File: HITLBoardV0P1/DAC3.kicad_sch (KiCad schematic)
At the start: 13 parts, among them U16 NC7SZ04P5X, U17 SN74LVC1G08DCKR, U18 DAC7750IPWPR

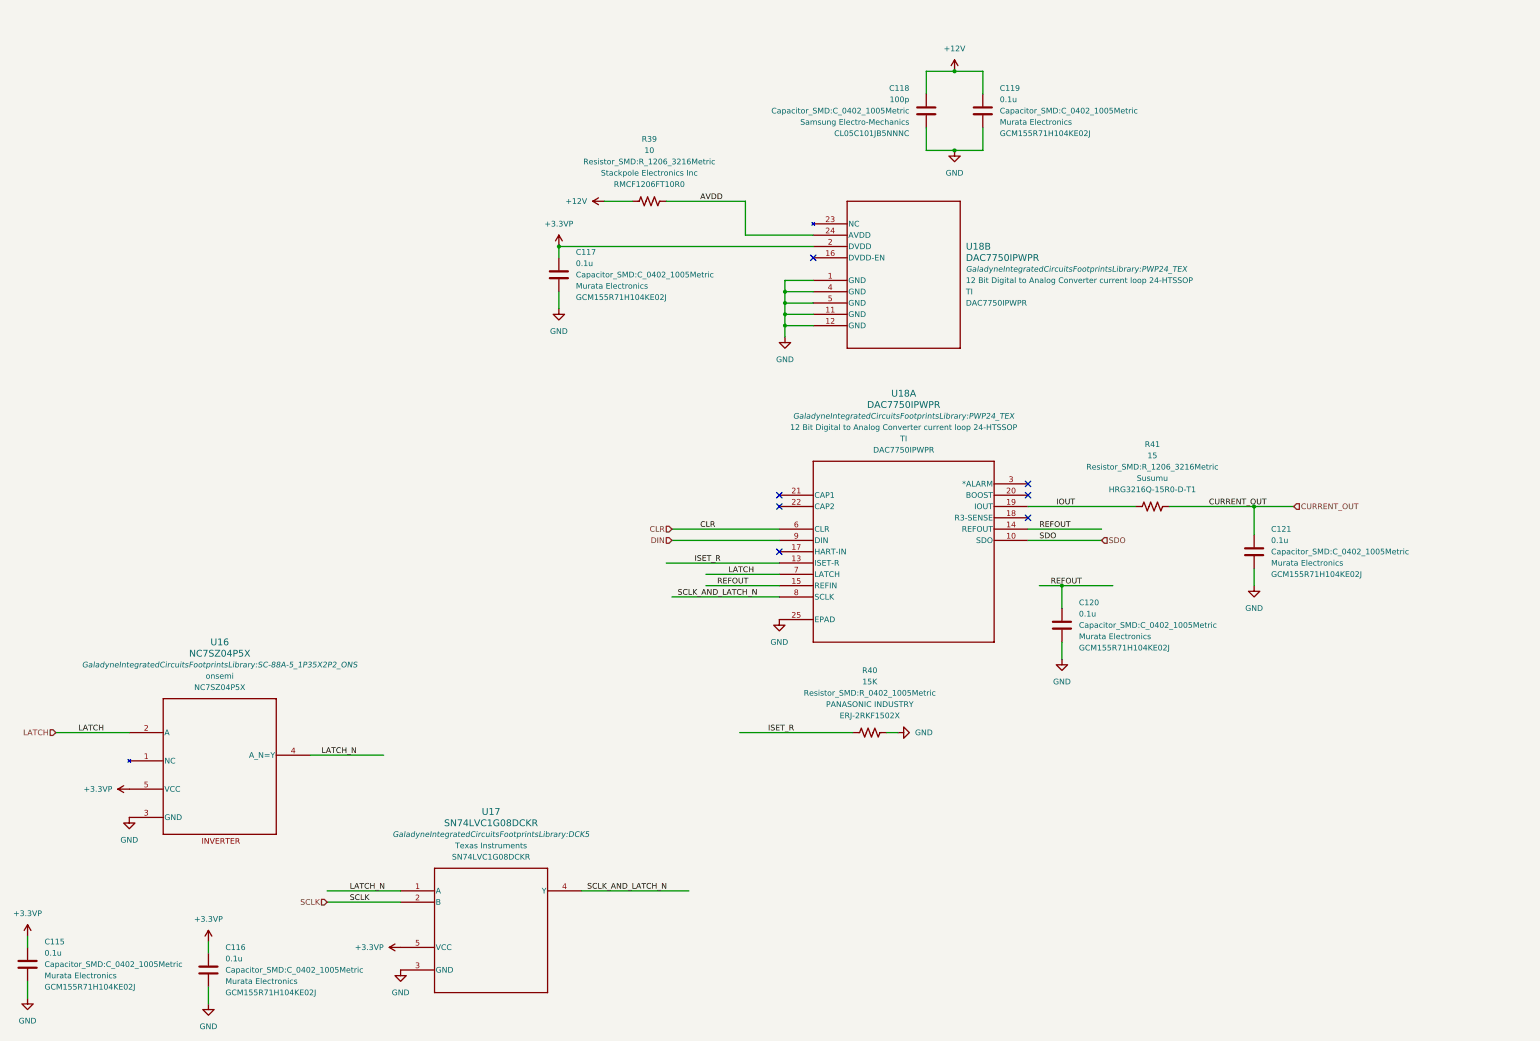
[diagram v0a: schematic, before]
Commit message: update to board with spi buses assigned
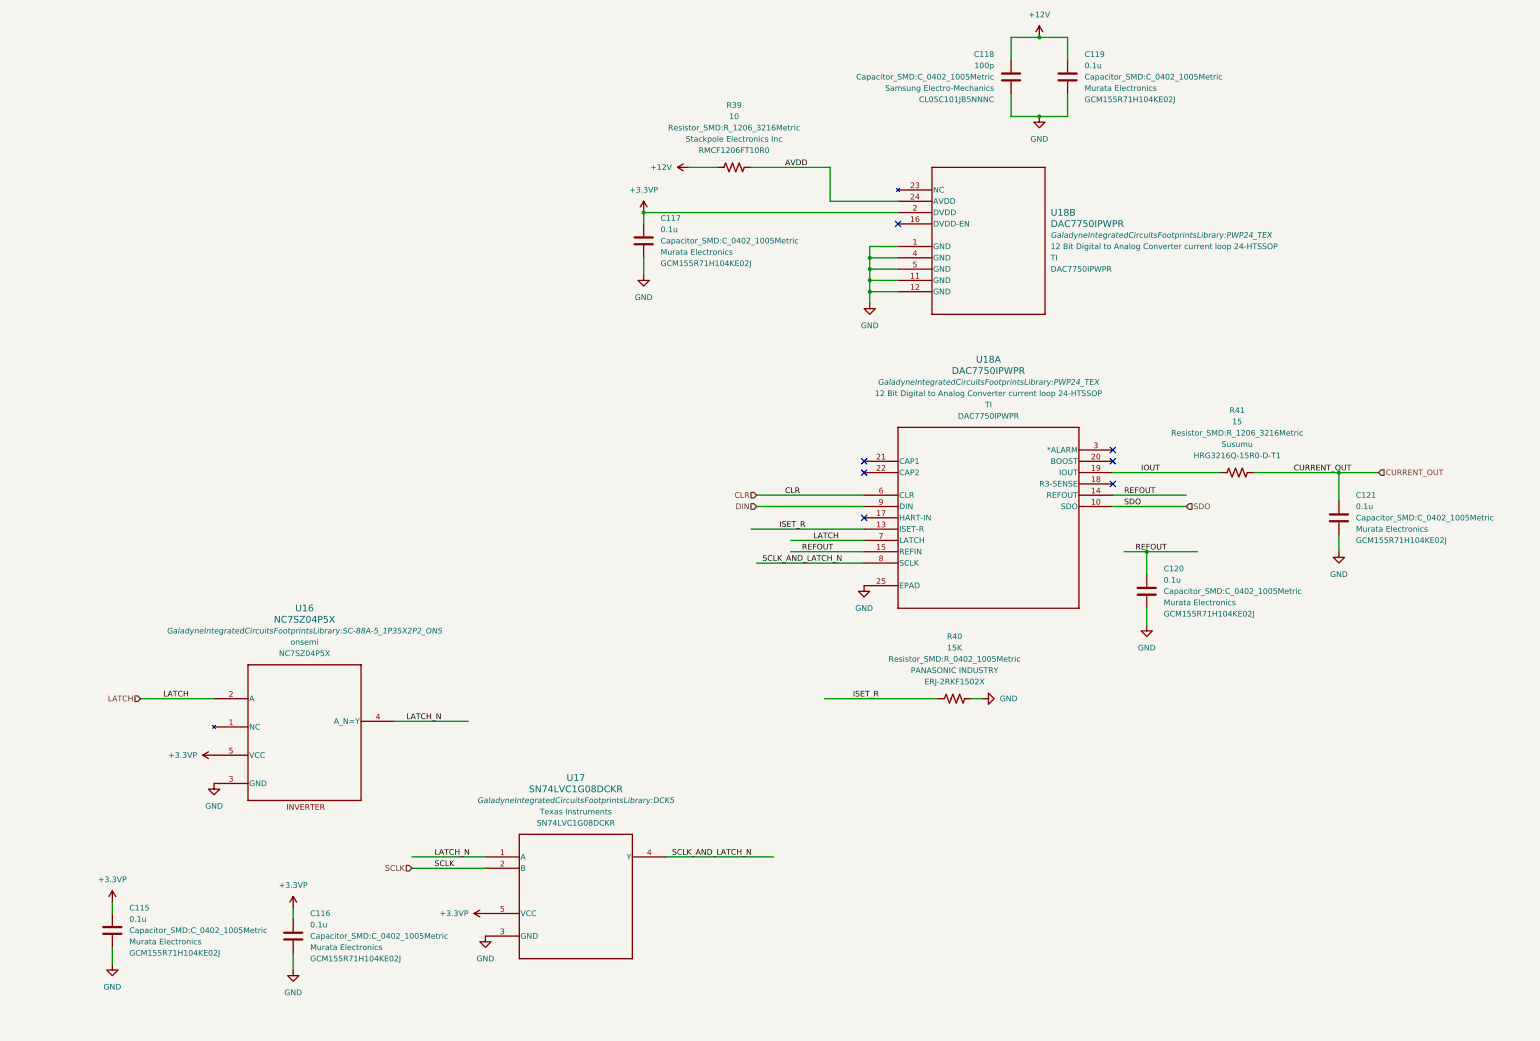
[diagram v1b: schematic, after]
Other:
- moved on the sheet: C115, C116, C117, C118, C119, C120, C121, R39, R40, R41, U16, U17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
